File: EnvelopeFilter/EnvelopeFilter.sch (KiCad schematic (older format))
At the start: 58 parts, among them J1 Conn_01x02_Male, J2 Conn_01x03_Male, J3 Conn_01x03_Male, J4 Conn_01x03_Male, J5 Conn_01x03_Male, J6 Conn_01x03_Male, J7 Conn_01x03_Male, J8 Conn_01x03_Male, J9 Conn_01x09_Male, U1 AS3320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

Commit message: Minor EnvelopeFilter changes, created SummingAmp
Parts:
- added C11, C12: 100uF, Capacitor_THT:CP_Radial_D8.0mm_P3.50mm, symbol Device:CP
- C1, C3, C4, C9: value 1n -> 1nF
- C10: value 1u -> 1uF
- C5, R11: value 10n -> 10nF
- C7: value 33n -> 33nF
- C8: value 0.1u -> 0.1uF
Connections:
- net +15V: now also C11.1
- net -15V: now also C12.2
- net GND: now also C11.2, C12.1
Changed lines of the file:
@@
 P 5300 6250
 F 0 "C5" H 5185 6204 50  0000 R CNN
-F 1 "10n" H 5185 6295 50  0000 R CNN
+F 1 "10nF" H 5185 6295 50  0000 R CNN
 F 2 "Capacitor_THT:C_Disc_D4.3mm_W1.9mm_P5.00mm" H 5338 6100 50  0001 C CNN
 F 3 "~" H 5300 6250 50  0001 C CNN
@@
 P 5950 6750
 F 0 "C7" H 6200 6750 50  0000 R CNN
-F 1 "33n" H 6200 6850 50  0000 R CNN
+F 1 "33nF" H 6200 6850 50  0000 R CNN
 F 2 "Capacitor_THT:C_Disc_D4.3mm_W1.9mm_P5.00mm" H 5988 6600 50  0001 C CNN
 F 3 "~" H 5950 6750 50  0001 C CNN
@@
 P 2950 4550
 F 0 "R11" H 2835 4504 50  0000 R CNN
-F 1 "10n" H 2835 4595 50  0000 R CNN
+F 1 "10nF" H 2835 4595 50  0000 R CNN
 F 2 "Resistor_THT:R_Axial_DIN0204_L3.6mm_D1.6mm_P5.08mm_Horizontal" H 2988 4400 50  0001 C CNN
 F 3 "~" H 2950 4550 50  0001 C CNN
@@
 P 6750 4050
 F 0 "C8" H 6650 4000 50  0000 R CNN
-F 1 "0.1u" H 6650 4100 50  0000 R CNN
+F 1 "0.1uF" H 6650 4100 50  0000 R CNN
 F 2 "Capacitor_THT:C_Disc_D4.3mm_W1.9mm_P5.00mm" H 6788 3900 50  0001 C CNN
 F 3 "~" H 6750 4050 50  0001 C CNN
@@
 P 7550 2550
 F 0 "C9" H 7750 2500 50  0000 R CNN
-F 1 "1n" H 7750 2600 50  0000 R CNN
+F 1 "1nF" H 7750 2600 50  0000 R CNN
 F 2 "Capacitor_THT:C_Disc_D4.3mm_W1.9mm_P5.00mm" H 7588 2400 50  0001 C CNN
 F 3 "~" H 7550 2550 50  0001 C CNN
@@
 P 5150 2300
 F 0 "C4" V 5400 2350 50  0000 R CNN
-F 1 "1n" V 5300 2350 50  0000 R CNN
+F 1 "1nF" V 5300 2350 50  0000 R CNN
 F 2 "Capacitor_THT:C_Disc_D4.3mm_W1.9mm_P5.00mm" H 5188 2150 50  0001 C CNN
 F 3 "~" H 5150 2300 50  0001 C CNN
@@
 P 1750 2300
 F 0 "C1" V 2000 2350 50  0000 R CNN
-F 1 "1n" V 1900 2350 50  0000 R CNN
+F 1 "1nF" V 1900 2350 50  0000 R CNN
 F 2 "Capacitor_THT:C_Disc_D4.3mm_W1.9mm_P5.00mm" H 1788 2150 50  0001 C CNN
 F 3 "~" H 1750 2300 50  0001 C CNN
@@
 P 3300 2300
 F 0 "C3" V 3550 2350 50  0000 R CNN
-F 1 "1n" V 3450 2350 50  0000 R CNN
+F 1 "1nF" V 3450 2350 50  0000 R CNN
 F 2 "Capacitor_THT:C_Disc_D4.3mm_W1.9mm_P5.00mm" H 3338 2150 50  0001 C CNN
 F 3 "~" H 3300 2300 50  0001 C CNN
@@
 P 8400 4550
 F 0 "C10" H 8300 4500 50  0000 R CNN
-F 1 "1u" H 8300 4600 50  0000 R CNN
+F 1 "1uF" H 8300 4600 50  0000 R CNN
 F 2 "Capacitor_THT:C_Disc_D4.3mm_W1.9mm_P5.00mm" H 8438 4400 50  0001 C CNN
 F 3 "~" H 8400 4550 50  0001 C CNN
@@
 Wire Wire Line
 	9250 3200 10300 3200
+$Comp
+L Device:CP C11
+U 1 1 5FDBBE78
+P 10100 1550
+F 0 "C11" H 10218 1596 50  0000 L CNN
+F 1 "100uF" H 10218 1505 50  0000 L CNN
+F 2 "Capacitor_THT:CP_Radial_D8.0mm_P3.50mm" H 10138 1400 50  0001 C CNN
+F 3 "~" H 10100 1550 50  0001 C CNN
+	1    10100 1550
+	1    0    0    -1
+$EndComp
+$Comp
+L Device:CP C12
+U 1 1 5FDBD02B
+P 10100 2050
+F 0 "C12" H 10218 2096 50  0000 L CNN
+F 1 "100uF" H 10218 2005 50  0000 L CNN
+F 2 "Capacitor_THT:CP_Radial_D8.0mm_P3.50mm" H 10138 1900 50  0001 C CNN
+F 3 "~" H 10100 2050 50  0001 C CNN
+	1    10100 2050
+	1    0    0    -1
+$EndComp
+$Comp
+L power:-15V #PWR0101
+U 1 1 5FDBDA24
+P 10100 2300
+F 0 "#PWR0101" H 10100 2400 50  0001 C CNN
+F 1 "-15V" H 10115 2473 50  0000 C CNN
+F 2 "" H 10100 2300 50  0001 C CNN
+F 3 "" H 10100 2300 50  0001 C CNN
+	1    10100 2300
+	-1   0    0    1
+$EndComp
+$Comp
+L power:+15V #PWR0102
+U 1 1 5FDBE4BF
+P 10100 1300
+F 0 "#PWR0102" H 10100 1150 50  0001 C CNN
+F 1 "+15V" H 10115 1473 50  0000 C CNN
+F 2 "" H 10100 1300 50  0001 C CNN
+F 3 "" H 10100 1300 50  0001 C CNN
+	1    10100 1300
+	1    0    0    -1
+$EndComp
+$Comp
+L power:GND #PWR0103
+U 1 1 5FDBEF5E
+P 9800 1900
+F 0 "#PWR0103" H 9800 1650 50  0001 C CNN
+F 1 "GND" H 9805 1727 50  0000 C CNN
+F 2 "" H 9800 1900 50  0001 C CNN
+F 3 "" H 9800 1900 50  0001 C CNN
+	1    9800 1900
+	-1   0    0    -1
+$EndComp
+Wire Wire Line
+	10100 1300 10100 1400
+Wire Wire Line
+	10100 1700 10100 1800
+Wire Wire Line
+	10100 1800 9800 1800
+Wire Wire Line
+	9800 1800 9800 1900
+Wire Wire Line
+	10100 2300 10100 2200
+Wire Wire Line
+	10100 1900 10100 1800
+Connection ~ 10100 1800
 $EndSCHEMATC

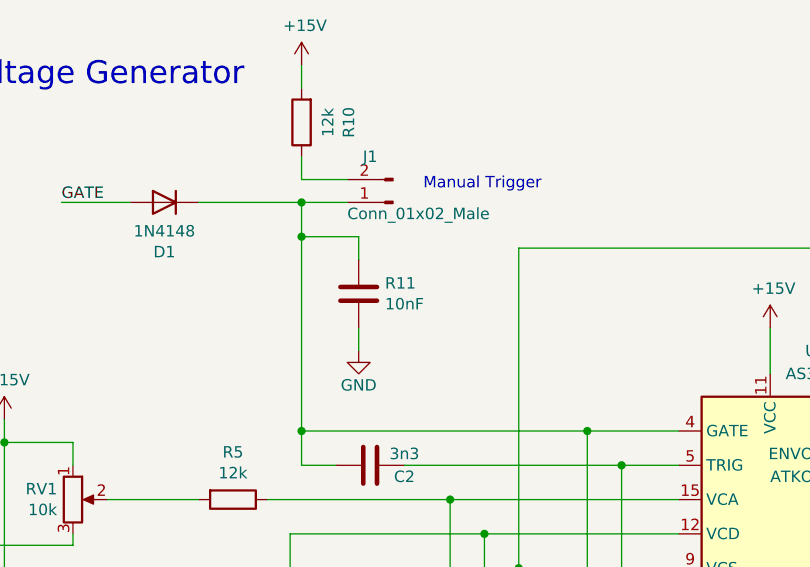
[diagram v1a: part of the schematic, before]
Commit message: Reannotated R11 -> C13 in Filter
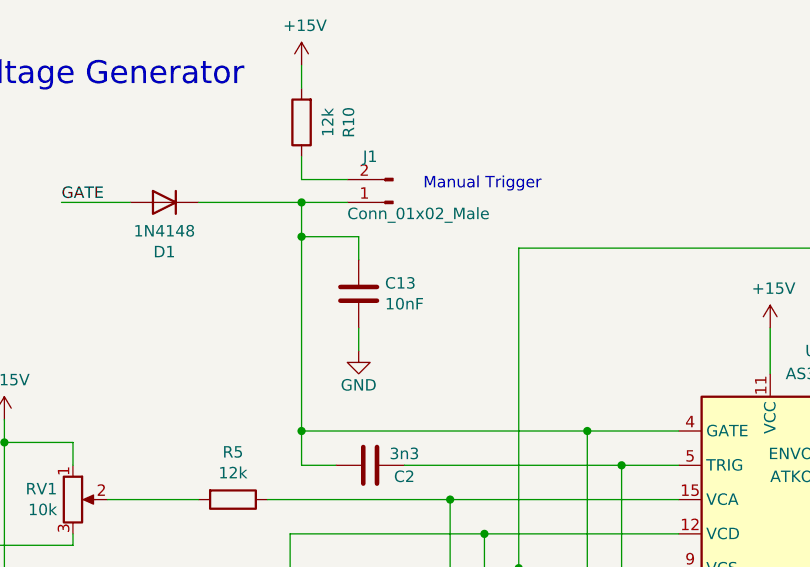
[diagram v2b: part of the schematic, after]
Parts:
- renumbered R11 to C13
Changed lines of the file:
@@
 	3650 6950 3800 6950
 $Comp
-L Device:C R11
+L Device:C C13
 U 1 1 5FE1841F
 P 2950 4550
-F 0 "R11" H 2835 4504 50  0000 R CNN
+F 0 "C13" H 2835 4504 50  0000 R CNN
 F 1 "10nF" H 2835 4595 50  0000 R CNN
 F 2 "Resistor_THT:R_Axial_DIN0204_L3.6mm_D1.6mm_P5.08mm_Horizontal" H 2988 4400 50  0001 C CNN

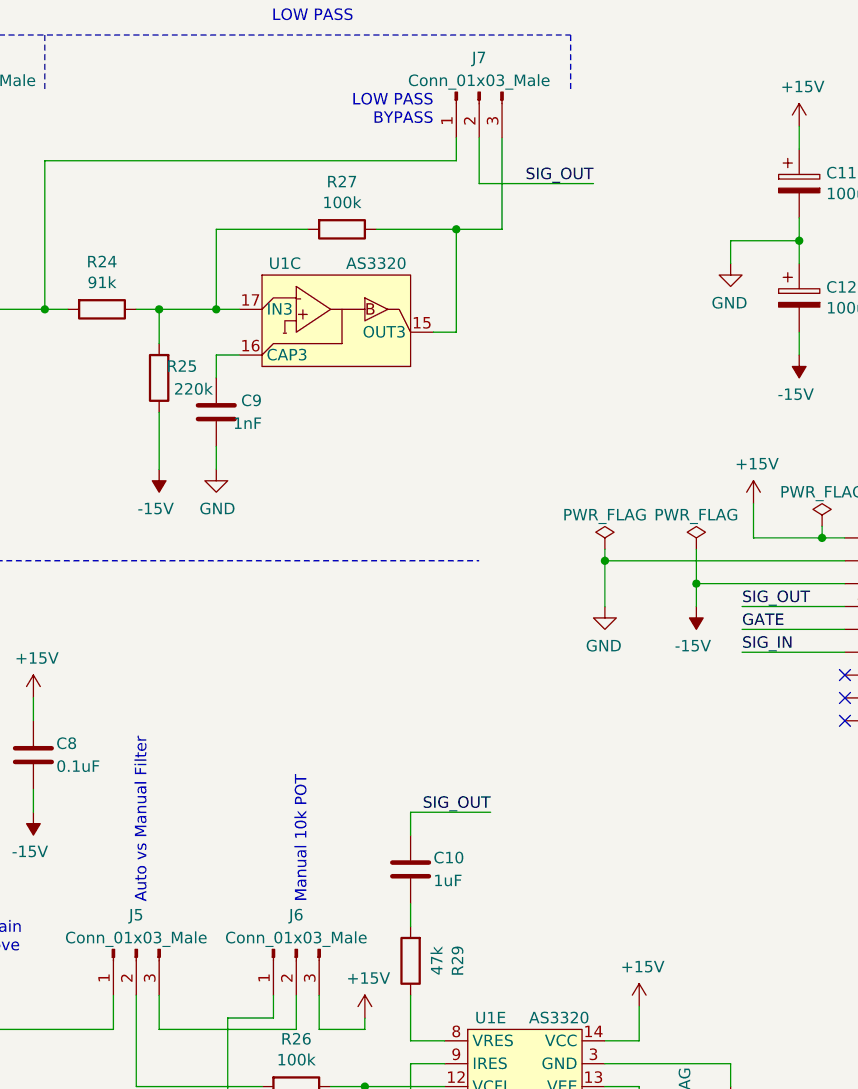
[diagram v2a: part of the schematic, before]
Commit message: Resolved Issue #3 Also: * Added output cap to 555 modules * EnvelopeFilter now has an output cap
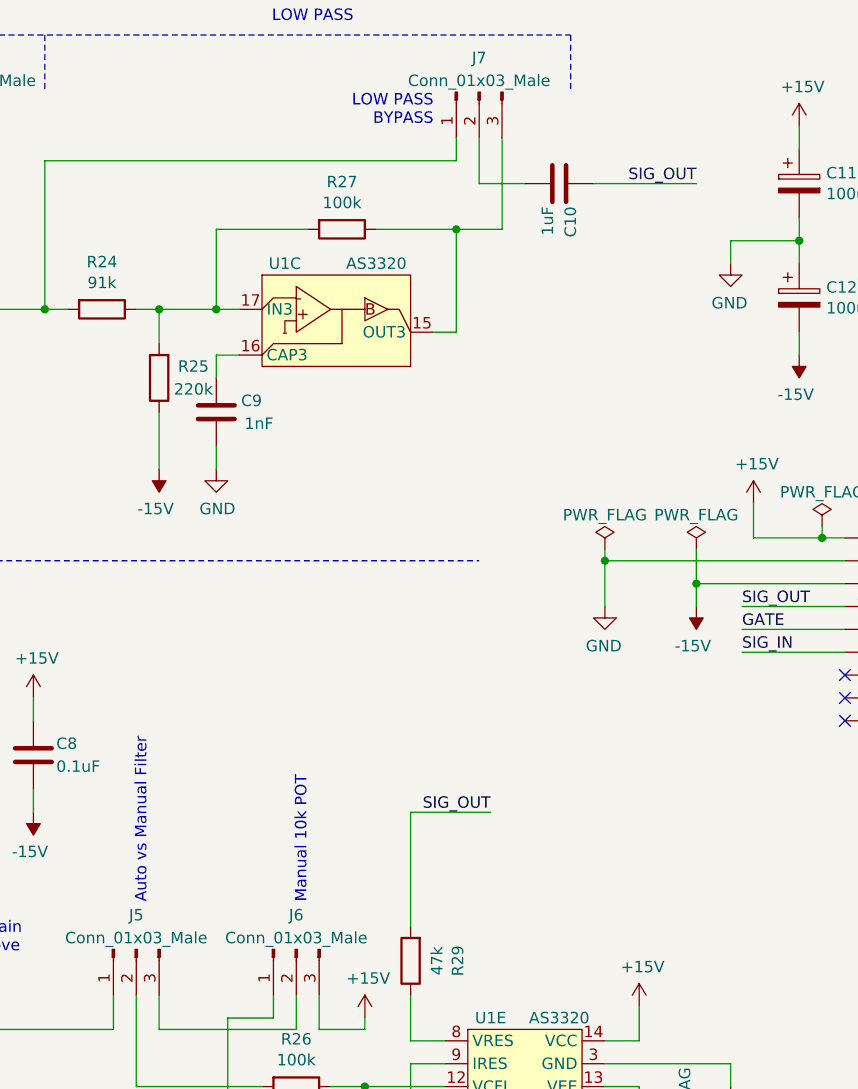
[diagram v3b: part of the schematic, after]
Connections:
- net SIG_OUT: now also R29.2; no longer J7.2 (Pin_2)
- net at C10.1: now also J7.2 (Pin_2); no longer R29.2
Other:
- moved on the sheet: C10
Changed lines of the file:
@@
 P 7550 2550
 F 0 "C9" H 7750 2500 50  0000 R CNN
-F 1 "1nF" H 7750 2600 50  0000 R CNN
+F 1 "1nF" H 7800 2600 50  0000 R CNN
 F 2 "Capacitor_THT:C_Disc_D4.3mm_W1.9mm_P5.00mm" H 7588 2400 50  0001 C CNN
 F 3 "~" H 7550 2550 50  0001 C CNN
@@
 U 1 1 607DD3EF
 P 7300 2400
-F 0 "R25" H 7200 2350 50  0000 C CNN
+F 0 "R25" H 7150 2350 50  0000 C CNN
 F 1 "220k" H 7150 2450 50  0000 C CNN
 F 2 "Resistor_THT:R_Axial_DIN0204_L3.6mm_D1.6mm_P5.08mm_Horizontal" V 7230 2400 50  0001 C CNN
@@
 Wire Wire Line
 	4700 1350 4700 1550
-Text Label 9200 1550 2    50   ~ 0
+Text Label 9650 1550 2    50   ~ 0
 SIG_OUT
 Connection ~ 8600 1750
@@
 Wire Wire Line
 	4900 1550 4700 1550
-Wire Wire Line
-	8700 1550 9200 1550
 Wire Wire Line
 	6450 2100 6800 2100
@@
 L Device:C C10
 U 1 1 611D5E3E
-P 8400 4550
-F 0 "C10" H 8300 4500 50  0000 R CNN
-F 1 "1uF" H 8300 4600 50  0000 R CNN
-F 2 "Capacitor_THT:C_Disc_D4.3mm_W1.9mm_P5.00mm" H 8438 4400 50  0001 C CNN
-F 3 "~" H 8400 4550 50  0001 C CNN
-	1    8400 4550
-	-1   0    0    1
-$EndComp
-Wire Wire Line
-	8400 4400 8400 4300
+P 9050 1550
+F 0 "C10" H 8950 1500 50  0000 R CNN
+F 1 "1uF" H 8950 1600 50  0000 R CNN
+F 2 "Capacitor_THT:C_Disc_D4.3mm_W1.9mm_P5.00mm" H 9088 1400 50  0001 C CNN
+F 3 "~" H 9050 1550 50  0001 C CNN
+	1    9050 1550
+	0    -1   -1   0
+$EndComp
 Wire Wire Line
 	8400 4300 8750 4300
-Wire Wire Line
-	8400 4700 8400 4800
 Wire Wire Line
 	8550 5400 8400 5400
@@
 	10100 1900 10100 1800
 Connection ~ 10100 1800
+Wire Wire Line
+	8700 1550 8900 1550
+Wire Wire Line
+	9200 1550 9650 1550
+Wire Wire Line
+	8400 4300 8400 4800
 $EndSCHEMATC

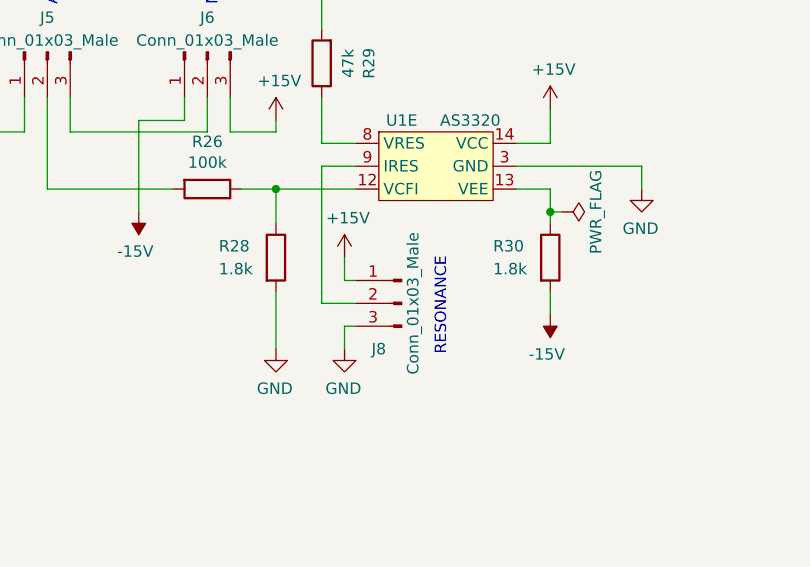
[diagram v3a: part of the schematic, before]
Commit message: Added resonance current limit resistor
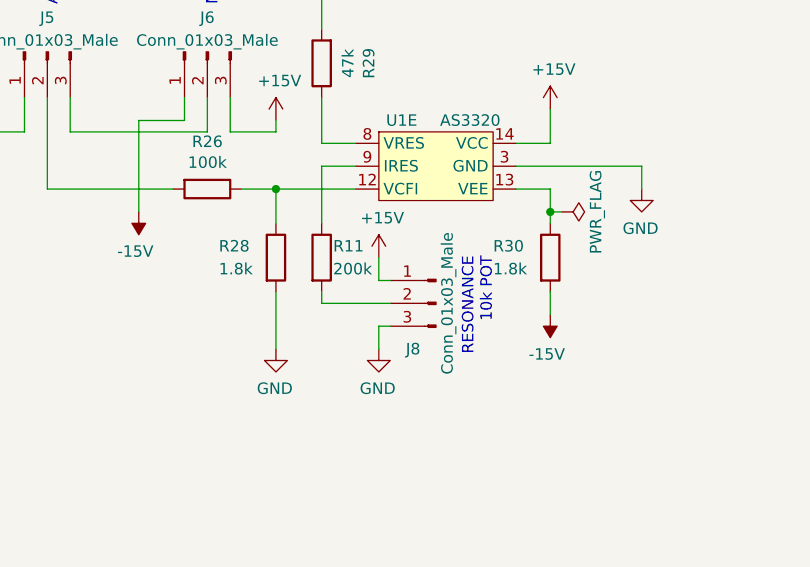
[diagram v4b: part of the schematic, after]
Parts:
- added R11: 200k, Resistor_THT:R_Axial_DIN0204_L3.6mm_D1.6mm_P5.08mm_Horizontal, symbol Device:R
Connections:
- net at U1.9 (IRES): now also R11.1; no longer J8.2 (Pin_2)
- new net: J8.2 (Pin_2), R11.2
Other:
- note added: "RESONANCE\n10k POT\n"
- note removed: "RESONANCE"
- moved on the sheet: J8
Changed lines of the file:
@@
 L Connector:Conn_01x03_Male J8
 U 1 1 6075B45A
-P 8750 6000
-F 0 "J8" H 8850 5800 50  0000 C CNN
-F 1 "Conn_01x03_Male" V 8700 6000 50  0000 C CNN
-F 2 "Connector_PinHeader_2.54mm:PinHeader_1x03_P2.54mm_Vertical" H 8750 6000 50  0001 C CNN
-F 3 "~" H 8750 6000 50  0001 C CNN
-	1    8750 6000
+P 8900 6000
+F 0 "J8" H 9000 5800 50  0000 C CNN
+F 1 "Conn_01x03_Male" V 8850 6000 50  0000 C CNN
+F 2 "Connector_PinHeader_2.54mm:PinHeader_1x03_P2.54mm_Vertical" H 8900 6000 50  0001 C CNN
+F 3 "~" H 8900 6000 50  0001 C CNN
+	1    8900 6000
 	-1   0    0    -1
 $EndComp
@@
 	8550 5400 8400 5400
 Wire Wire Line
-	8400 5400 8400 6000
-Wire Wire Line
-	8400 6000 8550 6000
-Wire Wire Line
-	8550 5900 8500 5900
-Wire Wire Line
-	8500 5900 8500 5800
-Wire Wire Line
-	8550 6100 8500 6100
-Wire Wire Line
-	8500 6100 8500 6200
+	8400 5400 8400 5650
+Wire Wire Line
+	8700 5900 8650 5900
+Wire Wire Line
+	8650 5900 8650 5800
+Wire Wire Line
+	8700 6100 8650 6100
+Wire Wire Line
+	8650 6100 8650 6200
 $Comp
 L power:GND #PWR025
 U 1 1 612370E0
-P 8500 6200
-F 0 "#PWR025" H 8500 5950 50  0001 C CNN
-F 1 "GND" H 8505 6027 50  0000 C CNN
-F 2 "" H 8500 6200 50  0001 C CNN
-F 3 "" H 8500 6200 50  0001 C CNN
-	1    8500 6200
+P 8650 6200
+F 0 "#PWR025" H 8650 5950 50  0001 C CNN
+F 1 "GND" H 8655 6027 50  0000 C CNN
+F 2 "" H 8650 6200 50  0001 C CNN
+F 3 "" H 8650 6200 50  0001 C CNN
+	1    8650 6200
 	-1   0    0    -1
 $EndComp
@@
 L power:+15V #PWR024
 U 1 1 612375B3
-P 8500 5800
-F 0 "#PWR024" H 8500 5650 50  0001 C CNN
-F 1 "+15V" H 8515 5973 50  0000 C CNN
-F 2 "" H 8500 5800 50  0001 C CNN
-F 3 "" H 8500 5800 50  0001 C CNN
-	1    8500 5800
+P 8650 5800
+F 0 "#PWR024" H 8650 5650 50  0001 C CNN
+F 1 "+15V" H 8665 5973 50  0000 C CNN
+F 2 "" H 8650 5800 50  0001 C CNN
+F 3 "" H 8650 5800 50  0001 C CNN
+	1    8650 5800
 	1    0    0    -1
 $EndComp
@@
 Text Notes 7950 4700 1    50   ~ 0
 Manual 10k POT
-Text Notes 8950 5800 3    50   ~ 0
-RESONANCE
+Text Notes 9150 5800 3    50   ~ 0
+RESONANCE\n10k POT\n
 $Comp
 L power:PWR_FLAG #FLG0101
@@
 Wire Wire Line
 	8400 4300 8400 4800
+$Comp
+L Device:R R11
+U 1 1 60180B80
+P 8400 5800
+F 0 "R11" H 8450 5850 50  0000 L CNN
+F 1 "200k" H 8450 5750 50  0000 L CNN
+F 2 "Resistor_THT:R_Axial_DIN0204_L3.6mm_D1.6mm_P5.08mm_Horizontal" V 8330 5800 50  0001 C CNN
+F 3 "~" H 8400 5800 50  0001 C CNN
+	1    8400 5800
+	1    0    0    -1
+$EndComp
+Wire Wire Line
+	8400 5950 8400 6000
+Wire Wire Line
+	8400 6000 8700 6000
 $EndSCHEMATC
